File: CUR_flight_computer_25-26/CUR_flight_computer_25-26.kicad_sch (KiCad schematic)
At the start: 0 parts

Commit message: Try this
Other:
- added sheet Debug (debug.kicad_sch)
- added sheet Flash (flash.kicad_sch)
- added sheet GPS (gps.kicad_sch)
- added sheet MCU (MCU.kicad_sch)
- added sheet Peripherals (peripherals.kicad_sch)
- added sheet Power (power.kicad_sch)
- added sheet Pyro (pyro.kicad_sch)
- added sheet Sensors (sensors.kicad_sch)
- added sheet Telemetry (telemetry.kicad_sch)
- added sheet USB (usb.kicad_sch)

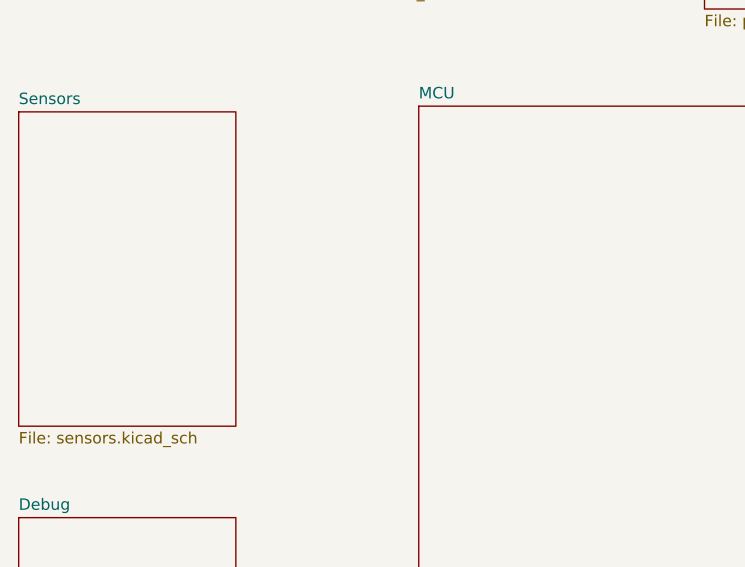
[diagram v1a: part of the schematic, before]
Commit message: Baro schematic
Hooked up 4-wire SPI
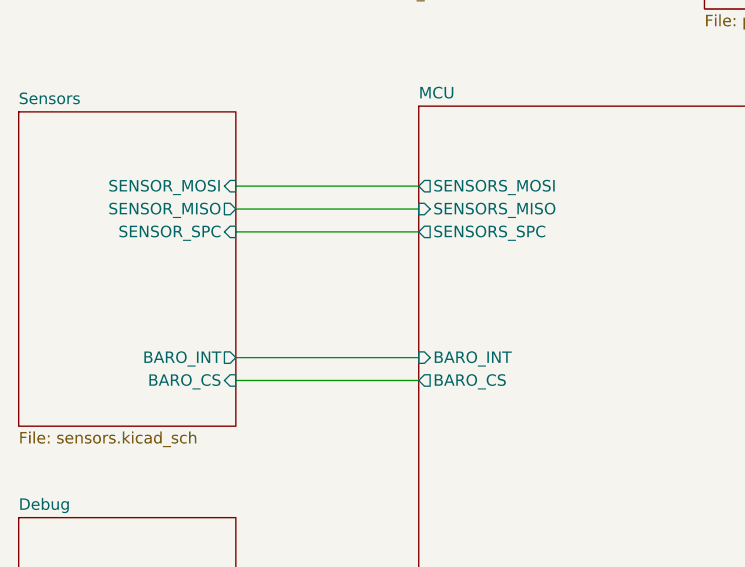
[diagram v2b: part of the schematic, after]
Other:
- sheet MCU ports: added BARO_CS, BARO_INT, SENSORS_MISO, SENSORS_MOSI, SENSORS_SPC; removed none
- sheet Sensors ports: added BARO_CS, BARO_INT, SENSOR_MISO, SENSOR_MOSI, SENSOR_SPC; removed none
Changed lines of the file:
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@@
 	(generator_version "9.0")
 	(paper "A4")
+	(wire
+		(pts
+			(xy 93.98 82.55) (xy 114.3 82.55)
+		)
+		(stroke
+			(width 0)
+			(type default)
+		)
+	)
+	(wire
+		(pts
+			(xy 93.98 80.01) (xy 114.3 80.01)
+		)
+		(stroke
+			(width 0)
+			(type default)
+		)
+	)
+	(wire
+		(pts
+			(xy 93.98 66.04) (xy 114.3 66.04)
+		)
+		(stroke
+			(width 0)
+			(type default)
+		)
+	)
+	(wire
+		(pts
+			(xy 93.98 63.5) (xy 114.3 63.5)
+		)
+		(stroke
+			(width 0)
+			(type default)
+		)
+	)
+	(wire
+		(pts
+			(xy 93.98 60.96) (xy 114.3 60.96)
+		)
+		(stroke
+			(width 0)
+			(type default)
+		)
+	)
 	(sheet
 		(at 69.85 97.79)
@@
 			)
 		)
+		(pin "SENSORS_MISO" input
+			(at 114.3 63.5 180)
+			(effects
+				(font
+					(size 1.27 1.27)
+				)
+				(justify left)
+			)
+		)
+		(pin "SENSORS_MOSI" output
+			(at 114.3 60.96 180)
+			(effects
+				(font
+					(size 1.27 1.27)
+				)
+				(justify left)
+			)
+		)
+		(pin "SENSORS_SPC" output
+			(at 114.3 66.04 180)
+			(effects
+				(font
+					(size 1.27 1.27)
+				)
+				(justify left)
+			)
+		)
+		(pin "BARO_INT" input
+			(at 114.3 80.01 180)
+			(effects
+				(font
+					(size 1.27 1.27)
+				)
+				(justify left)
+			)
+		)
+		(pin "BARO_CS" output
+			(at 114.3 82.55 180)
+			(effects
+				(font
+					(size 1.27 1.27)
+				)
+				(justify left)
+			)
+		)
 		(instances
 			(project "CUR_flight_computer_25-26"
@@
 			)
 		)
+		(pin "BARO_CS" input
+			(at 93.98 82.55 0)
+			(effects
+				(font
+					(size 1.27 1.27)
+				)
+				(justify right)
+			)
+		)
+		(pin "SENSOR_SPC" input
+			(at 93.98 66.04 0)
+			(effects
+				(font
+					(size 1.27 1.27)
+				)
+				(justify right)
+			)
+		)
+		(pin "BARO_INT" output
+			(at 93.98 80.01 0)
+			(effects
+				(font
+					(size 1.27 1.27)
+				)
+				(justify right)
+			)
+		)
+		(pin "SENSOR_MISO" output
+			(at 93.98 63.5 0)
+			(effects
+				(font
+					(size 1.27 1.27)
+				)
+				(justify right)
+			)
+		)
+		(pin "SENSOR_MOSI" input
+			(at 93.98 60.96 0)
+			(effects
+				(font
+					(size 1.27 1.27)
+				)
+				(justify right)
+			)
+		)

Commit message: Magnitomer
Put In Magnitominer
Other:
- sheet MCU ports: added MAG_CLOCK, MAG_CS, MAG_DATA, MAG_INT; removed none
- sheet Sensors ports: added MAG CLOCK, MAG_CS, MAG_DATA, MAG_INT; removed none
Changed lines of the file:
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@@
+	(wire
+		(pts
+			(xy 93.98 77.47) (xy 114.3 77.47)
+		)
+		(stroke
+			(width 0)
+			(type default)
+		)
+	)
+	(wire
+		(pts
+			(xy 93.98 69.85) (xy 114.3 69.85)
+		)
+		(stroke
+			(width 0)
+			(type default)
+		)
+	)
 	(wire
 		(pts
@@
 		(pts
 			(xy 93.98 60.96) (xy 114.3 60.96)
+		)
+		(stroke
+			(width 0)
+			(type default)
+		)
+	)
+	(wire
+		(pts
+			(xy 93.98 74.93) (xy 114.3 74.93)
+		)
+		(stroke
+			(width 0)
+			(type default)
+		)
+	)
+	(wire
+		(pts
+			(xy 93.98 72.39) (xy 114.3 72.39)
 		)
 		(stroke
@@
 			)
 		)
+		(pin "MAG_CLOCK" output
+			(at 114.3 77.47 180)
+			(effects
+				(font
+					(size 1.27 1.27)
+				)
+				(justify left)
+			)
+		)
+		(pin "MAG_CS" output
+			(at 114.3 74.93 180)
+			(effects
+				(font
+					(size 1.27 1.27)
+				)
+				(justify left)
+			)
+		)
+		(pin "MAG_DATA" bidirectional
+			(at 114.3 72.39 180)
+			(effects
+				(font
+					(size 1.27 1.27)
+				)
+				(justify left)
+			)
+		)
+		(pin "MAG_INT" input
+			(at 114.3 69.85 180)
+			(effects
+				(font
+					(size 1.27 1.27)
+				)
+				(justify left)
+			)
+		)
 		(instances
 			(project "CUR_flight_computer_25-26"
@@
 			(effects
 				(font
+					(size 1.27 1.27)
+				)
+				(justify right)
+			)
+		)
+		(pin "MAG CLOCK" input
+			(at 93.98 77.47 0)
+			(effects
+				(font
+					(size 1.27 1.27)
+				)
+				(justify right)
+			)
+		)
+		(pin "MAG_CS" input
+			(at 93.98 74.93 0)
+			(effects
+				(font
+					(size 1.27 1.27)
+				)
+				(justify right)
+			)
+		)
+		(pin "MAG_DATA" bidirectional
+			(at 93.98 72.39 0)
+			(effects
+				(font
+					(size 1.27 1.27)
+				)
+				(justify right)
+			)
+		)
+		(pin "MAG_INT" output
+			(at 93.98 69.85 0)
+			(effects
+				(font

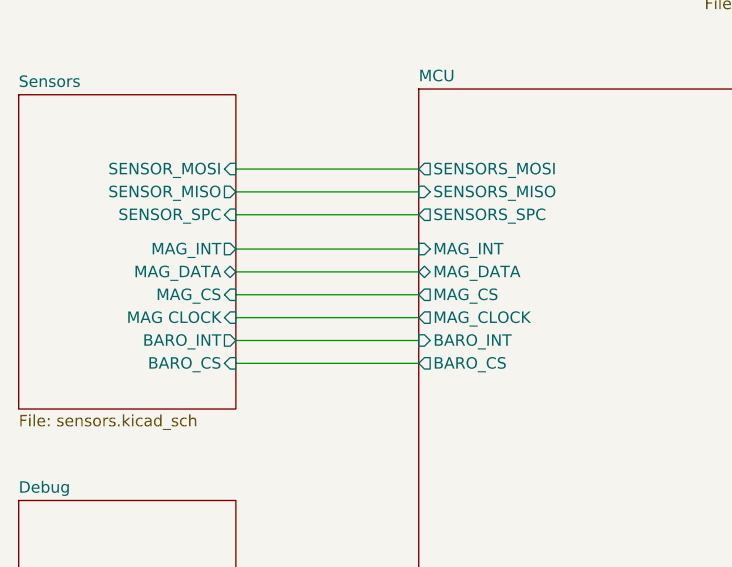
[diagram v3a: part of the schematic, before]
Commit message: Revert "Magnitomer"
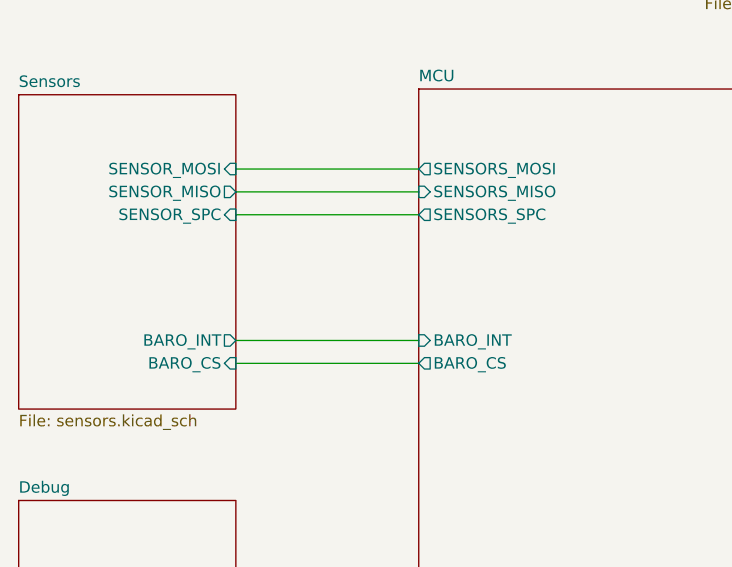
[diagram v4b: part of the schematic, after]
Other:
- sheet MCU ports: added none; removed MAG_CLOCK, MAG_CS, MAG_DATA, MAG_INT
- sheet Sensors ports: added none; removed MAG CLOCK, MAG_CS, MAG_DATA, MAG_INT
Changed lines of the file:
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@@
-	(wire
-		(pts
-			(xy 93.98 77.47) (xy 114.3 77.47)
-		)
-		(stroke
-			(width 0)
-			(type default)
-		)
-	)
-	(wire
-		(pts
-			(xy 93.98 69.85) (xy 114.3 69.85)
-		)
-		(stroke
-			(width 0)
-			(type default)
-		)
-	)
 	(wire
 		(pts
@@
 		)
 	)
-	(wire
-		(pts
-			(xy 93.98 74.93) (xy 114.3 74.93)
-		)
-		(stroke
-			(width 0)
-			(type default)
-		)
-	)
-	(wire
-		(pts
-			(xy 93.98 72.39) (xy 114.3 72.39)
-		)
-		(stroke
-			(width 0)
-			(type default)
-		)
-	)
 	(sheet
 		(at 69.85 97.79)
@@
 			)
 		)
-		(pin "MAG_CLOCK" output
-			(at 114.3 77.47 180)
-			(effects
-				(font
-					(size 1.27 1.27)
-				)
-				(justify left)
-			)
-		)
-		(pin "MAG_CS" output
-			(at 114.3 74.93 180)
-			(effects
-				(font
-					(size 1.27 1.27)
-				)
-				(justify left)
-			)
-		)
-		(pin "MAG_DATA" bidirectional
-			(at 114.3 72.39 180)
-			(effects
-				(font
-					(size 1.27 1.27)
-				)
-				(justify left)
-			)
-		)
-		(pin "MAG_INT" input
-			(at 114.3 69.85 180)
-			(effects
-				(font
-					(size 1.27 1.27)
-				)
-				(justify left)
-			)
-		)
 		(instances
 			(project "CUR_flight_computer_25-26"
@@
 			(effects
 				(font
-					(size 1.27 1.27)
-				)
-				(justify right)
-			)
-		)
-		(pin "MAG CLOCK" input
-			(at 93.98 77.47 0)
-			(effects
-				(font
-					(size 1.27 1.27)
-				)
-				(justify right)
-			)
-		)
-		(pin "MAG_CS" input
-			(at 93.98 74.93 0)
-			(effects
-				(font
-					(size 1.27 1.27)
-				)
-				(justify right)
-			)
-		)
-		(pin "MAG_DATA" bidirectional
-			(at 93.98 72.39 0)
-			(effects
-				(font
-					(size 1.27 1.27)
-				)
-				(justify right)
-			)
-		)
-		(pin "MAG_INT" output
-			(at 93.98 69.85 0)
-			(effects
-				(font

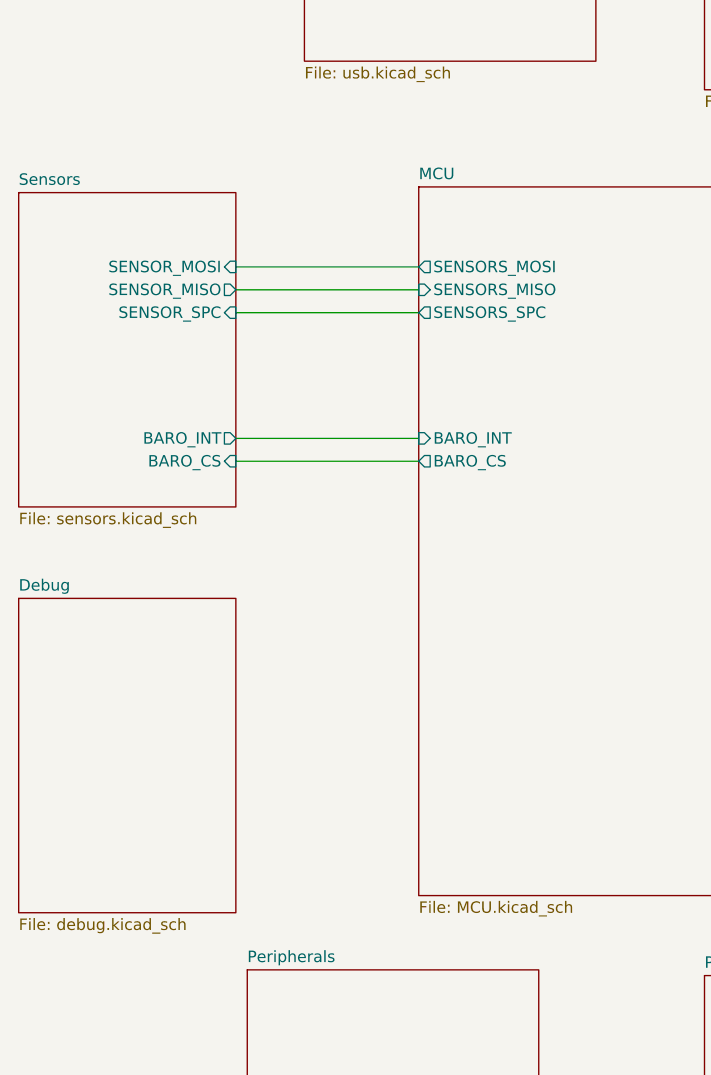
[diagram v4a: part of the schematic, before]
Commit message: fixes
fixed magnitometer
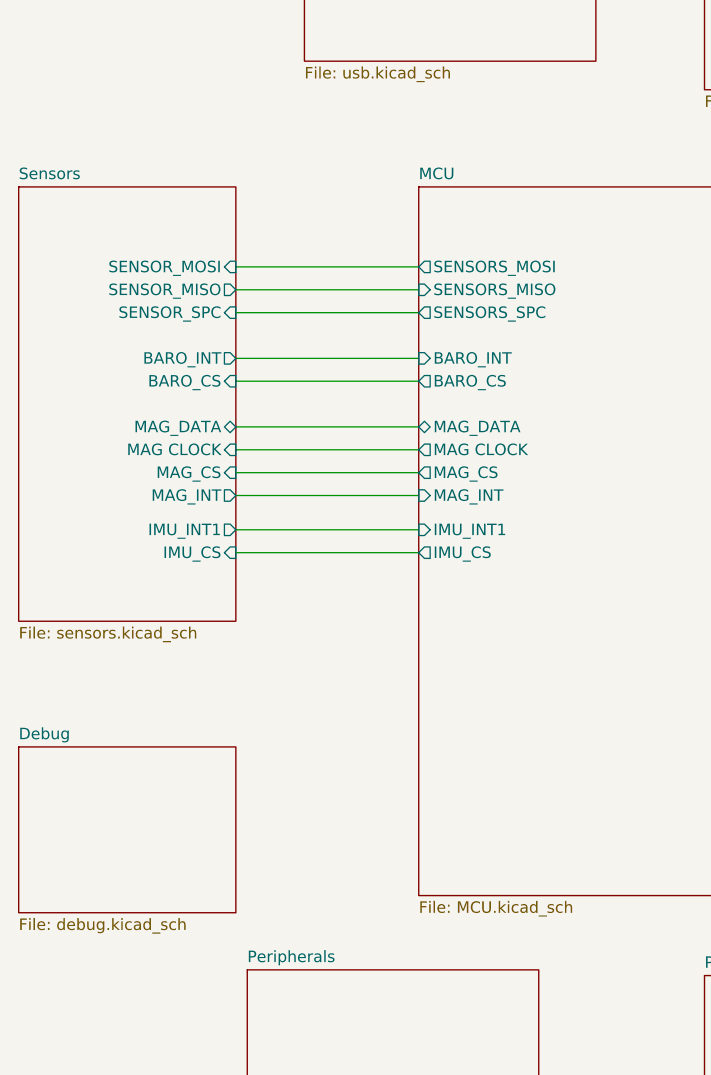
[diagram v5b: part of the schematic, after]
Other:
- sheet MCU ports: added IMU_CS, IMU_INT1, MAG CLOCK, MAG_CS, MAG_DATA, MAG_INT; removed none
- sheet Sensors ports: added IMU_CS, IMU_INT1, MAG CLOCK, MAG_CS, MAG_DATA, MAG_INT; removed none
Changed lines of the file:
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@@
 	(wire
 		(pts
-			(xy 93.98 82.55) (xy 114.3 82.55)
-		)
-		(stroke
-			(width 0)
-			(type default)
-		)
-	)
-	(wire
-		(pts
-			(xy 93.98 80.01) (xy 114.3 80.01)
+			(xy 93.98 78.74) (xy 114.3 78.74)
+		)
+		(stroke
+			(width 0)
+			(type default)
+		)
+	)
+	(wire
+		(pts
+			(xy 93.98 73.66) (xy 114.3 73.66)
+		)
+		(stroke
+			(width 0)
+			(type default)
+		)
+	)
+	(wire
+		(pts
+			(xy 93.98 71.12) (xy 114.3 71.12)
+		)
+		(stroke
+			(width 0)
+			(type default)
+		)
+	)
+	(wire
+		(pts
+			(xy 93.98 83.82) (xy 114.3 83.82)
 		)
 		(stroke
@@
 	(wire
 		(pts
+			(xy 93.98 92.71) (xy 114.3 92.71)
+		)
+		(stroke
+			(width 0)
+			(type default)
+		)
+	)
+	(wire
+		(pts
+			(xy 93.98 86.36) (xy 114.3 86.36)
+		)
+		(stroke
+			(width 0)
+			(type default)
+		)
+	)
+	(wire
+		(pts
 			(xy 93.98 60.96) (xy 114.3 60.96)
 		)
@@
 		)
 	)
-	(sheet
-		(at 69.85 97.79)
-		(size 24.13 34.925)
+	(wire
+		(pts
+			(xy 93.98 90.17) (xy 114.3 90.17)
+		)
+		(stroke
+			(width 0)
+			(type default)
+		)
+	)
+	(wire
+		(pts
+			(xy 93.98 81.28) (xy 114.3 81.28)
+		)
+		(stroke
+			(width 0)
+			(type default)
+		)
+	)
+	(sheet
+		(at 69.85 114.3)
+		(size 24.13 18.415)
 		(exclude_from_sim no)
 		(in_bom yes)
@@
 		)
 		(property "Sheetname" "Debug"
-			(at 69.85 97.0784 0)
+			(at 69.85 113.5884 0)
 			(effects
 				(font
@@
 		)
 		(pin "BARO_INT" input
-			(at 114.3 80.01 180)
+			(at 114.3 71.12 180)
 			(effects
 				(font
@@
 		)
 		(pin "BARO_CS" output
-			(at 114.3 82.55 180)
+			(at 114.3 73.66 180)
+			(effects
+				(font
+					(size 1.27 1.27)
+				)
+				(justify left)
+			)
+		)
+		(pin "MAG_DATA" bidirectional
+			(at 114.3 78.74 180)
+			(effects
+				(font
+					(size 1.27 1.27)
+				)
+				(justify left)
+			)
+		)
+		(pin "MAG_CS" output
+			(at 114.3 83.82 180)
+			(effects
+				(font
+					(size 1.27 1.27)
+				)
+				(justify left)
+			)
+		)
+		(pin "MAG CLOCK" output
+			(at 114.3 81.28 180)
+			(effects
+				(font
+					(size 1.27 1.27)
+				)
+				(justify left)
+			)
+		)
+		(pin "MAG_INT" input
+			(at 114.3 86.36 180)
+			(effects
+				(font
+					(size 1.27 1.27)
+				)
+				(justify left)
+			)
+		)
+		(pin "IMU_INT1" input
+			(at 114.3 90.17 180)
+			(effects
+				(font
+					(size 1.27 1.27)
+				)
+				(justify left)
+			)
+		)
+		(pin "IMU_CS" output
+			(at 114.3 92.71 180)
 			(effects
 				(font
@@
 	)
 	(sheet
-		(at 69.85 52.705)
-		(size 24.13 34.925)
+		(at 69.85 52.07)
+		(size 24.13 48.26)
 		(exclude_from_sim no)
 		(in_bom yes)
@@
 		)
 		(property "Sheetname" "Sensors"
-			(at 69.85 51.9934 0)
+			(at 69.85 51.3584 0)
 			(effects
 				(font
@@
 		)
 		(property "Sheetfile" "sensors.kicad_sch"
-			(at 69.85 88.2146 0)
+			(at 69.85 100.9146 0)
 			(effects
 				(font
@@
 		)
 		(pin "BARO_CS" input
-			(at 93.98 82.55 0)
+			(at 93.98 73.66 0)
 			(effects
 				(font
@@
 		)
 		(pin "BARO_INT" output
-			(at 93.98 80.01 0)
+			(at 93.98 71.12 0)
 			(effects
 				(font
@@
 			(effects
 				(font
+					(size 1.27 1.27)
+				)
+				(justify right)
+			)
+		)
+		(pin "MAG_DATA" bidirectional
+			(at 93.98 78.74 0)
+			(effects
+				(font
+					(size 1.27 1.27)
+				)
+				(justify right)
+			)
+		)
+		(pin "MAG CLOCK" input
+			(at 93.98 81.28 0)
+			(effects
+				(font
+					(size 1.27 1.27)
+				)
+				(justify right)
+			)
+		)
+		(pin "MAG_CS" input
+			(at 93.98 83.82 0)
+			(effects
+				(font
+					(size 1.27 1.27)
+				)
+				(justify right)
+			)
+		)
+		(pin "MAG_INT" output
+			(at 93.98 86.36 0)
+			(effects
+				(font
+					(size 1.27 1.27)
+				)
+				(justify right)
+			)
+		)
+		(pin "IMU_INT1" output
+			(at 93.98 90.17 0)
+			(effects
+				(font
+					(size 1.27 1.27)
+				)
+				(justify right)
+			)
+		)
+		(pin "IMU_CS" input
+			(at 93.98 92.71 0)
+			(effects
+				(font

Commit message: BUZZER
Stole it from Sig
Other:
- sheet MCU ports: added BUZZER; removed none
- sheet Peripherals ports: added BUZZER; removed none
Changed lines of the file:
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@@
+	(wire
+		(pts
+			(xy 114.3 123.19) (xy 107.95 123.19)
+		)
+		(stroke
+			(width 0)
+			(type default)
+		)
+	)
+	(wire
+		(pts
+			(xy 107.95 123.19) (xy 107.95 139.065)
+		)
+		(stroke
+			(width 0)
+			(type default)
+		)
+	)
 	(wire
 		(pts
@@
 			)
 		)
+		(pin "BUZZER" output
+			(at 114.3 123.19 180)
+			(effects
+				(font
+					(size 1.27 1.27)
+				)
+				(justify left)
+			)
+		)
 		(instances
 			(project "CUR_flight_computer_25-26"
@@
 			)
 		)
+		(pin "BUZZER" input
+			(at 107.95 139.065 90)
+			(effects
+				(font
+					(size 1.27 1.27)
+				)
+				(justify right)
+			)
+		)
